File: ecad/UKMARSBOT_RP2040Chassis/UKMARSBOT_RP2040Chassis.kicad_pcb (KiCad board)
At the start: 2 copper layers, 99.1 x 81.3 mm, 20 parts, among them J3 Conn_01x06, J4 Conn_01x06, J5 Conn_01x03, J6 POWER, J7 Switch, M1 CONN_06SILK_FEMALE_PTH, M1 Left MOTOR, M2  CONN_06SILK_FEMALE_PTH, M2 Right MOTOR, U2 LM7805_TO220

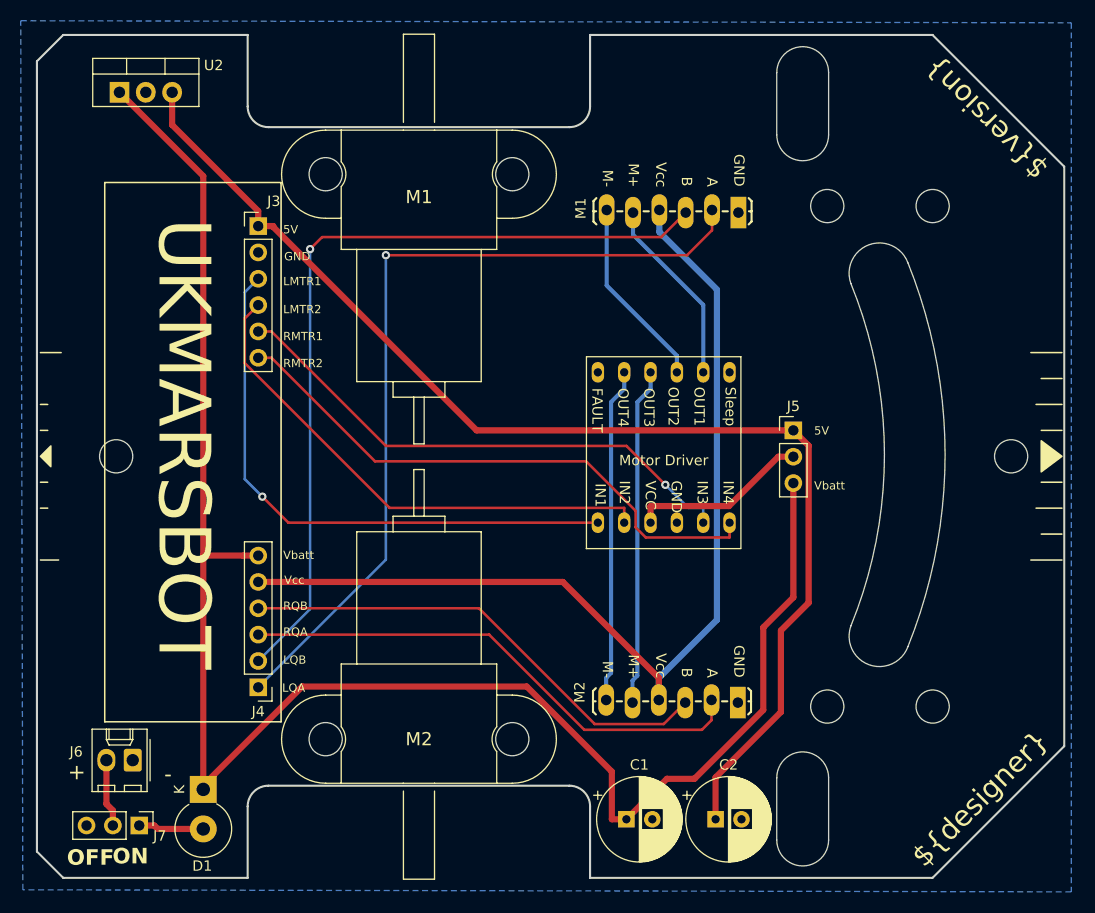
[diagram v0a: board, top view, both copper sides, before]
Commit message: Update to 5v rail and layouts across all 3 boards
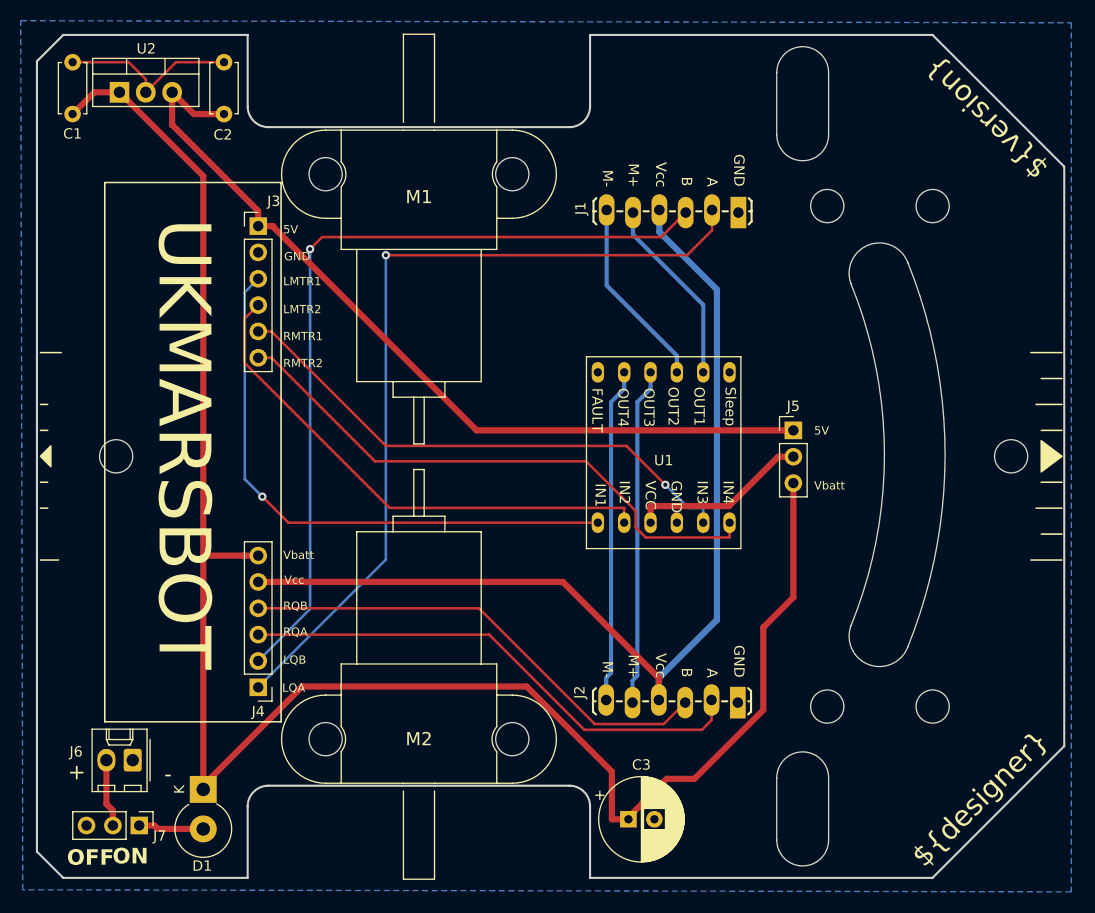
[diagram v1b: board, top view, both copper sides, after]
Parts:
- added C3: 330uF, 16V, Capacitor_THT:CP_Radial_D8.0mm_P2.50mm, F.Cu at (125.2, 140.0)
- C1: value 330uF, 16V -> 0.1uF, 16V; footprint Capacitor_THT:CP_Radial_D8.0mm_P2.50mm -> Capacitor_THT:C_Disc_D4.7mm_W2.5mm_P5.00mm
- C2: value 330uF, 16V -> 22uF, 16V; footprint Capacitor_THT:CP_Radial_D8.0mm_P2.50mm -> Capacitor_THT:C_Disc_D4.7mm_W2.5mm_P5.00mm
- J2: renamed from M2 
- U1: renamed from Motor Driver
- moved C1 86.5 mm to (71.6, 72.0), turned to 90 degrees
- moved C2 82.9 mm to (86.2, 72.0), turned to 90 degrees
- renumbered M1 to J1
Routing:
- net 5V: track 118.0 -> 82.0 mm
- net GND: track 0.00 -> 17.7 mm
- net Vbatt: track 169.6 -> 175.0 mm

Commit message: Capacitor smoothing. Chassis placement changes, Mez board made smaller and added an additional LED
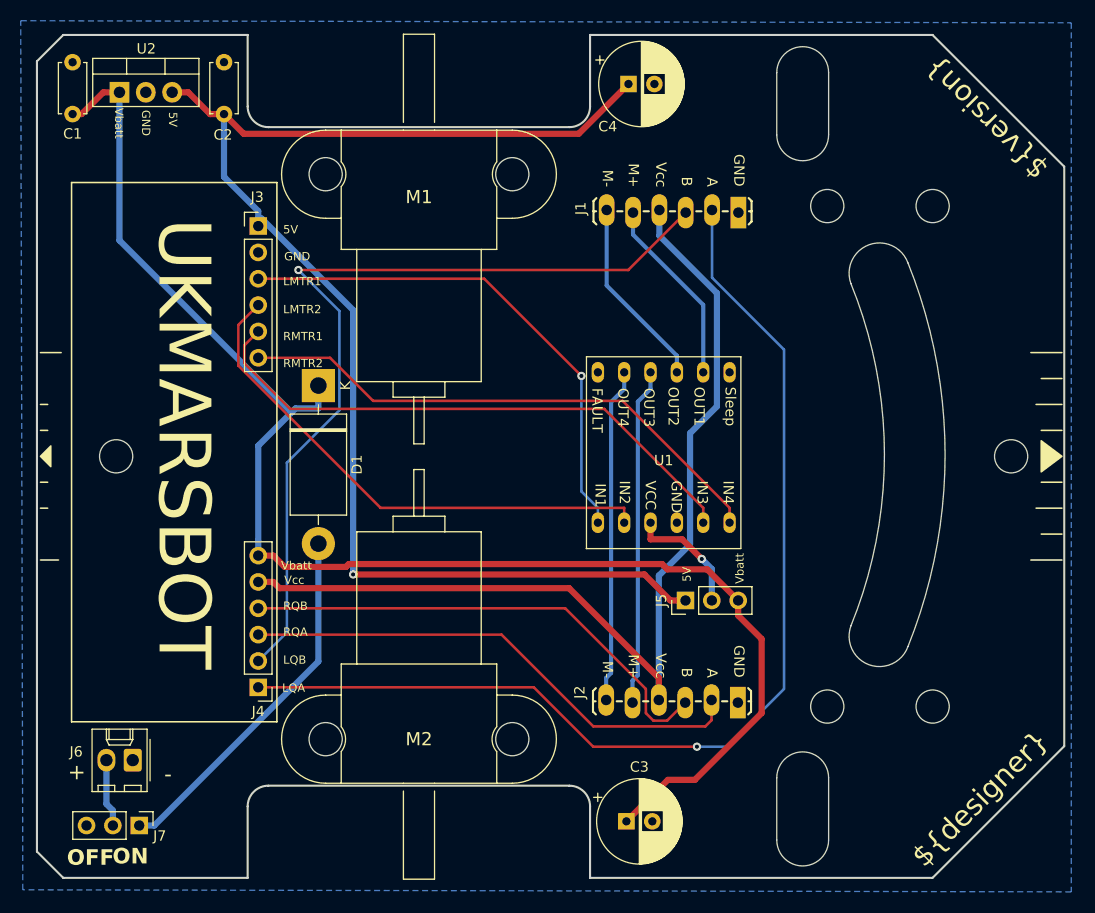
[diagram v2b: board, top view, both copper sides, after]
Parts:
- added C4: 330uF, 16V, Capacitor_THT:CP_Radial_D8.0mm_P2.50mm, F.Cu at (125.2, 69.1)
- C1: value 0.1uF, 16V -> 0.22uF
- C2: value 22uF, 16V -> 0.1uF
- D1: footprint Diode_THT:D_DO-201AE_P3.81mm_Vertical_KathodeUp -> Diode_THT:D_DO-201AD_P15.24mm_Horizontal
- moved D1 40.5 mm to (95.3, 98.2)
- moved J5 19.4 mm to (130.7, 118.9), turned to 90 degrees
- moved C3 0.28 mm to (125.0, 140.2)
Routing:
- net 5V: track 82.0 -> 131.2 mm, vias 0 -> 1
- net Vbatt: track 175.0 -> 140.7 mm
- net /PWR: track 6.31 -> 35.2 mm
- net LQA: track 81.2 -> 104.4 mm
- net GND: track 17.7 -> 0.00 mm
- net LMTR1: track 55.6 -> 49.9 mm
- net /PWR_motor: track 17.3 -> 11.7 mm, vias 0 -> 1
- net RMTR1: track 51.4 -> 55.1 mm, vias 1 -> 0
- net LQB: track 79.5 -> 82.2 mm
- net RMTR2: track 55.0 -> 52.9 mm
- net RQB: track 46.7 -> 47.7 mm
- net LMTR2: track 49.9 -> 50.9 mm

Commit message: Connectors moved to be on common 0.1" Grid and wheel cutouts included
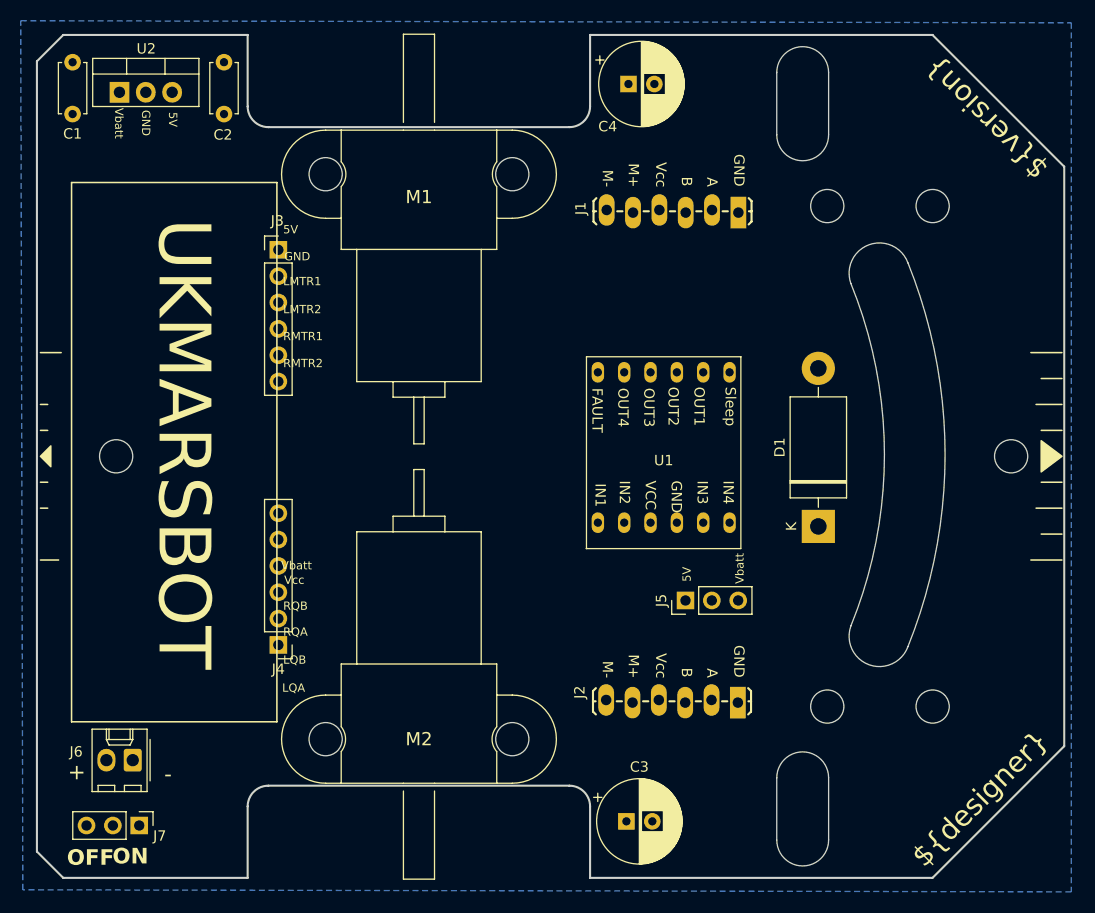
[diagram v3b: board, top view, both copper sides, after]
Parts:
- moved D1 50.1 mm to (143.5, 111.8), turned to 90 degrees
- moved J4 4.52 mm to (91.4, 123.2)
- moved J3 3.00 mm to (91.4, 85.1)
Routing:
- net Vbatt: track 140.7 -> 0.00 mm
- net 5V: track 131.2 -> 0.00 mm, vias 1 -> 0
- net LQA: track 104.4 -> 0.00 mm, vias 1 -> 0
- net Vcc: track 96.5 -> 0.00 mm
- net LQB: track 82.2 -> 0.00 mm, vias 1 -> 0
- net RMTR1: track 55.1 -> 0.00 mm
- net RMTR2: track 52.9 -> 0.00 mm
- net LMTR2: track 50.9 -> 0.00 mm
- net LMTR1: track 49.9 -> 0.00 mm, vias 1 -> 0
- net RQA: track 49.6 -> 0.00 mm
- net RQB: track 47.7 -> 0.00 mm
- net /PWR: track 35.2 -> 0.00 mm
- net RIGHT_MOTOR_1: track 32.6 -> 0.00 mm
- net RIGHT_MOTOR_2: track 32.3 -> 0.00 mm
- net LEFT_MOTOR_2: track 18.5 -> 0.00 mm
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
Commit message: Routed Chassis board with sleep pullup on motor bridge
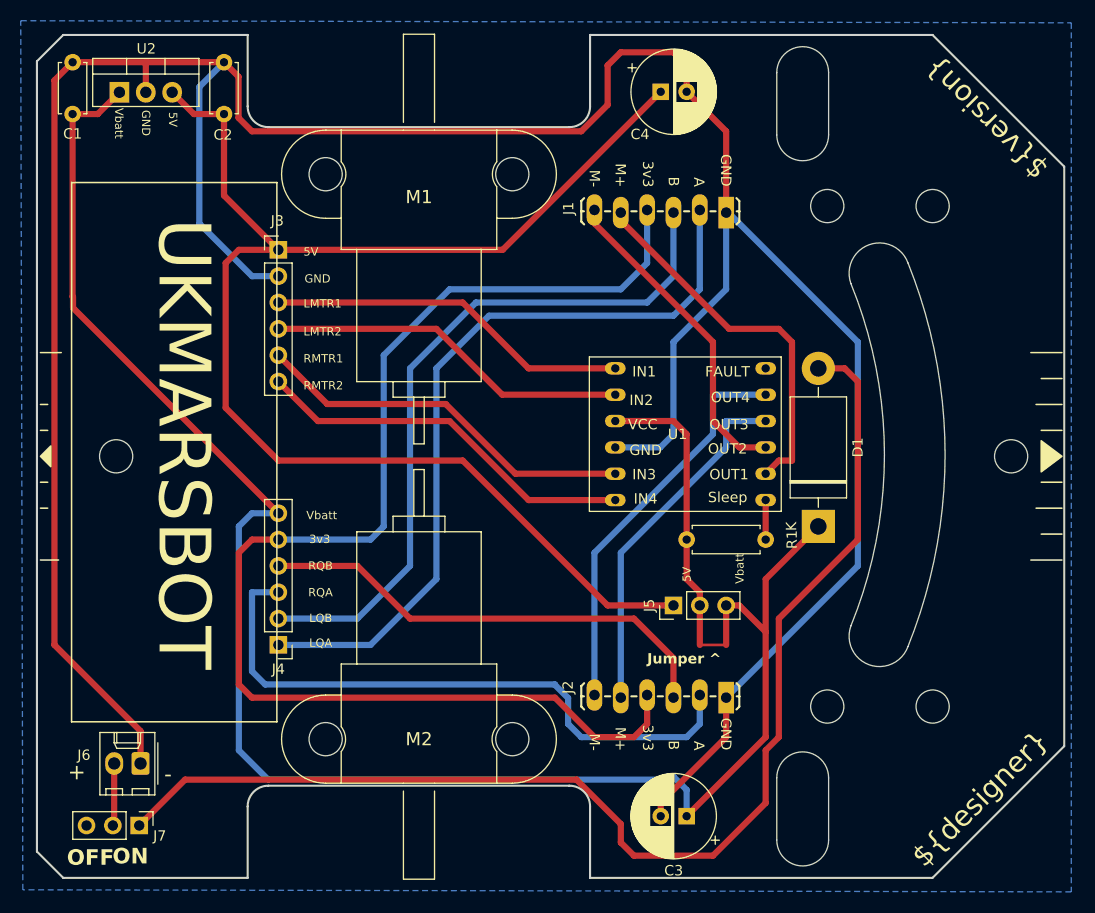
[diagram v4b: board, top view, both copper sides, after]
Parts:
- added R1: 47K, Resistor_THT:R_Axial_DIN0207_L6.3mm_D2.5mm_P7.62mm_Horizontal, F.Cu at (138.4, 113.0)
- moved C3 5.83 mm to (130.8, 139.7), turned to 180 degrees
- moved C4 3.20 mm to (128.3, 69.8)
- moved U1 2.86 mm to (129.9, 102.9), turned to 180 degrees
- moved J5 1.26 mm to (129.5, 119.4)
- moved J2 1.23 mm to (134.6, 128.3)
- moved J1 1.18 mm to (134.6, 81.5)
- moved J6 0.82 mm to (78.2, 134.6)
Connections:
- J5 pad 2: /PWR_motor -> Vbatt
- U1 pad 1: unconnected-(U1-SLEEP-Pad1) -> Net-(U1-SLEEP)
- U1 pad 9: /PWR_motor -> Vbatt
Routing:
- net GND: track 0.00 -> 288.0 mm
- net Vbatt: track 0.00 -> 198.2 mm
- net 5V: track 0.00 -> 135.0 mm
- net Vcc: track 0.00 -> 123.2 mm
- net /PWR: track 0.00 -> 117.1 mm
- net LQA: track 0.00 -> 74.4 mm
- net LQB: track 0.00 -> 69.1 mm
- net RQA: track 0.00 -> 60.8 mm
- net RQB: track 0.00 -> 45.6 mm
- net RIGHT_MOTOR_2: track 0.00 -> 38.8 mm
- net RMTR1: track 0.00 -> 37.2 mm
- net RMTR2: track 0.00 -> 37.2 mm
- net LEFT_MOTOR_1: track 0.00 -> 36.6 mm
- net LMTR2: track 0.00 -> 35.1 mm
- net LMTR1: track 0.00 -> 35.1 mm
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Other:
- board text added: "3v3"
- board text added: "Jumper ^"
- board text added: "Jumper^"
- board text removed: "Vcc"

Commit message: Routed Chassis and Mezzanine Boards
Position and orientate motor connections to allow use of JST-SH breakout connectors.  Position and orientate spare pin breakout to accomodate bluetooth module. Re-assign pins and orientate Pico to facilitate routing.
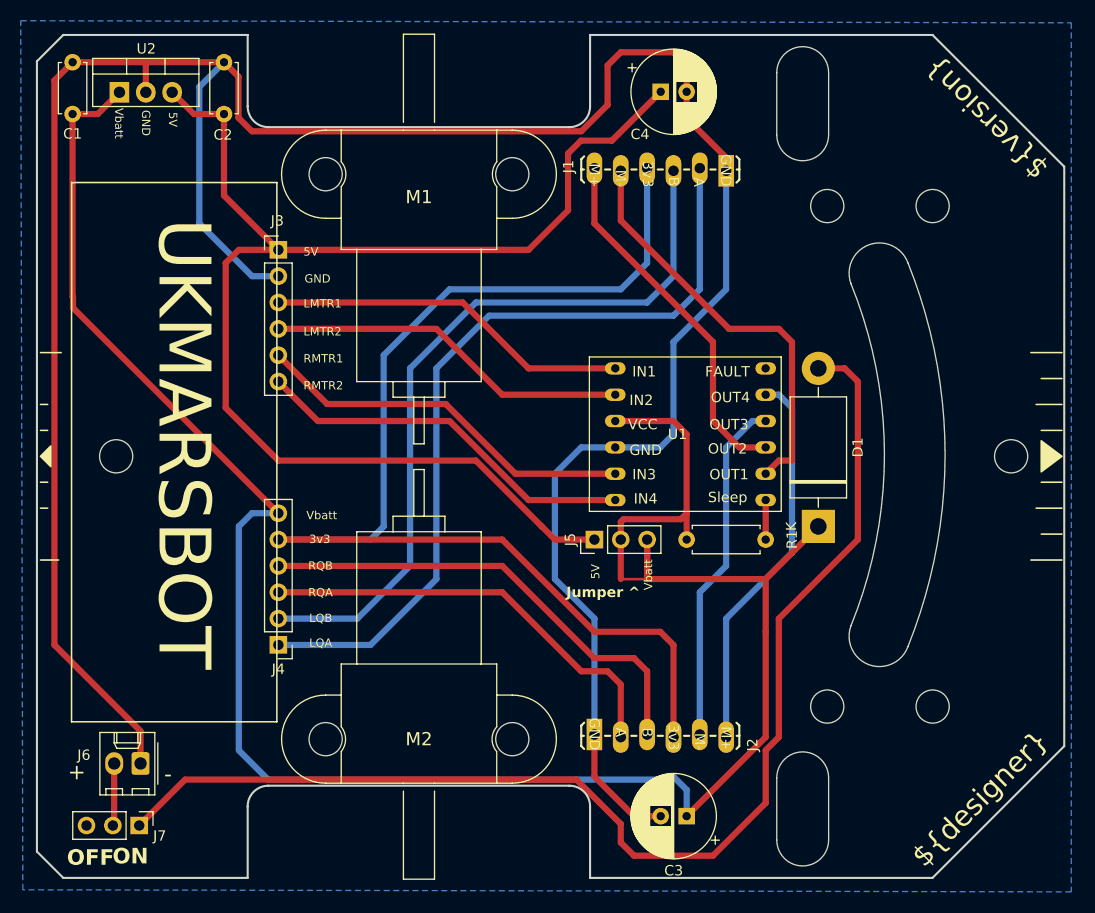
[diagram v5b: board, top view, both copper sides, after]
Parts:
- moved J2 13.2 mm to (121.9, 131.8), turned to 90 degrees
- moved J5 9.92 mm to (121.9, 113.0)
- moved J1 4.03 mm to (134.6, 77.5)
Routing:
- net GND: track 288.0 -> 262.2 mm
- net RQA: track 60.8 -> 41.8 mm
- net Vbatt: track 198.2 -> 210.1 mm
- net 5V: track 135.0 -> 127.9 mm
- net Vcc: track 123.2 -> 116.6 mm
- net LEFT_MOTOR_2: track 31.2 -> 35.3 mm
- net LQB: track 69.1 -> 73.1 mm
- net LQA: track 74.4 -> 78.4 mm
- net LEFT_MOTOR_1: track 36.6 -> 40.7 mm
- net RIGHT_MOTOR_2: track 38.8 -> 37.4 mm
- net RIGHT_MOTOR_1: track 34.7 -> 33.6 mm
